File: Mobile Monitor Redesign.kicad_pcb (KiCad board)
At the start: 4 copper layers, 49 x 39.1 mm, 92 parts, among them J1 Conn_01x02_Pin, J2 Conn_01x08_Pin, J3 Conn_01x08_Pin, J4 USB_C_Receptacle_USB2.0_16P, J5 Conn_02x03_Odd_Even, J7 Conn_01x05_Pin, J8 Conn_01x06_Socket, Q1 2N7002, Q2 AO3401A, Q5 AO3401A, Q6 2N7002, U1 ATmega2560-16A, U10 BQ27441DRZR-G1A, U11 TPL5010, U2 DS3232M, U5 XL4005, U6 IP5306, U7 CH340C, U8 FP6298XR, U9 AMS1117-3.3, Y1 Crystal_GND23

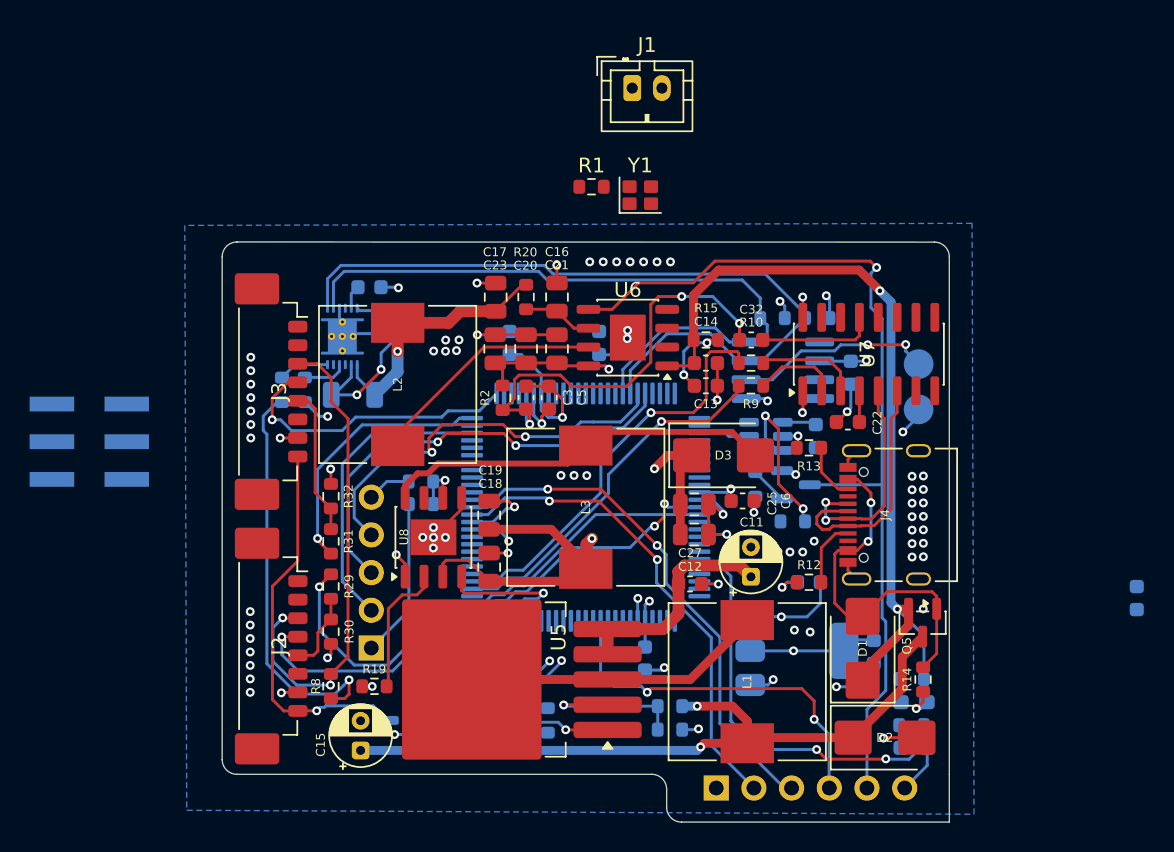
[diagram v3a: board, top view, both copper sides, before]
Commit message: cleaned up routes and added pads for SPI connections
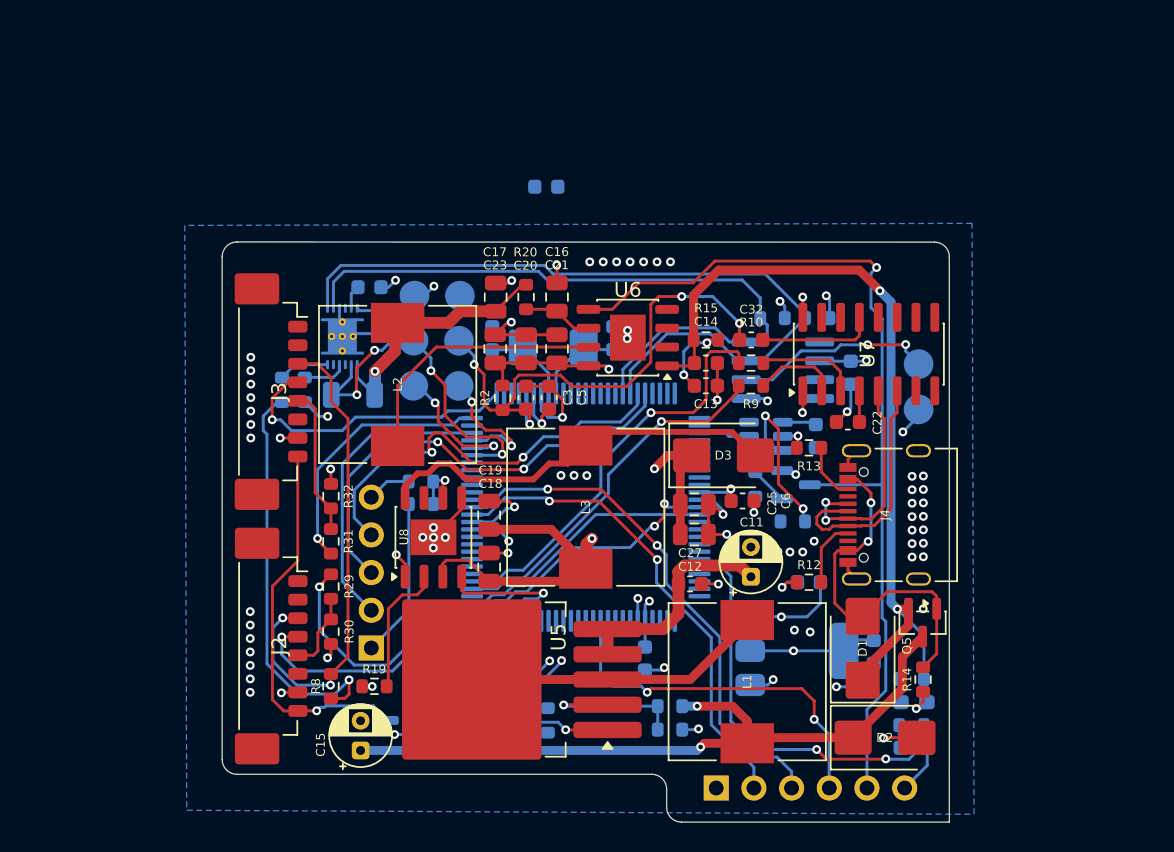
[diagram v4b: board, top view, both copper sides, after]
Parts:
- removed J1: Conn_01x02_Pin, Connector_JST:JST_PH_B2B-PH-K_1x02_P2.00mm_Vertical
- removed J5: Conn_02x03_Odd_Even, Connector_PinSocket_2.54mm:PinSocket_2x03_P2.54mm_Vertical_SMD
- removed R1: 1M, Resistor_SMD:R_0603_1608Metric
- removed Y1: Crystal_GND23, Crystal:Crystal_SMD_SeikoEpson_FA128-4Pin_2.0x1.6mm
- added 5V: TestPoint_Pad_D2.0mm, TestPoint:TestPoint_Pad_D2.0mm, B.Cu at (129.8, 84.8)
- added CLK: TestPoint_Pad_D2.0mm, TestPoint:TestPoint_Pad_D2.0mm, B.Cu at (129.8, 87.9)
- added GND: TestPoint_Pad_D2.0mm, TestPoint:TestPoint_Pad_D2.0mm, B.Cu at (132.9, 84.8)
- added MISO: TestPoint_Pad_D2.0mm, TestPoint:TestPoint_Pad_D2.0mm, B.Cu at (132.8, 90.9)
- added MOSI: TestPoint_Pad_D2.0mm, TestPoint:TestPoint_Pad_D2.0mm, B.Cu at (129.7, 90.9)
- added Y2: Crystal, Crystal:Crystal_SMD_Abracon_ABM3-2Pin_5.0x3.2mm, B.Cu at (139.2, 88.3)
- added rst: TestPoint_Pad_D2.0mm, TestPoint:TestPoint_Pad_D2.0mm, B.Cu at (132.8, 87.9)
- moved C30 48.5 mm to (138.7, 77.5), turned to 0 degrees
- moved C2 1.21 mm to (135.1, 87.7), turned to -90 degrees
- moved C1 1.00 mm to (143.2, 87.7), turned to 90 degrees
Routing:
- net SPI/CLK: track 0.00 -> 13.4 mm, vias 0 -> 2
- net SPI/MOSI: track 0.00 -> 9.25 mm, vias 0 -> 2
- net SPI/MISO: track 0.00 -> 9.19 mm, vias 0 -> 2
- net RESET: track 29.5 -> 35.9 mm, vias 3 -> 4
- net GND: track 107.3 -> 101.1 mm, vias 92 -> 87
- net Net-(U1-XTAL1): track 0.00 -> 6.03 mm
- net Net-(U1-XTAL2): track 0.00 -> 5.96 mm
- net /power/BATTERY_SEC: track 64.9 -> 67.0 mm
- net Net-(U6-SW): track 16.1 -> 18.0 mm
- net +5V: track 48.4 -> 50.0 mm, vias 12 -> 13
- net RXD1: track 27.3 -> 28.3 mm
- net Net-(D3-A): track 26.6 -> 27.5 mm
- net TXD1: track 30.6 -> 31.5 mm
- net TXD2: track 34.9 -> 35.6 mm

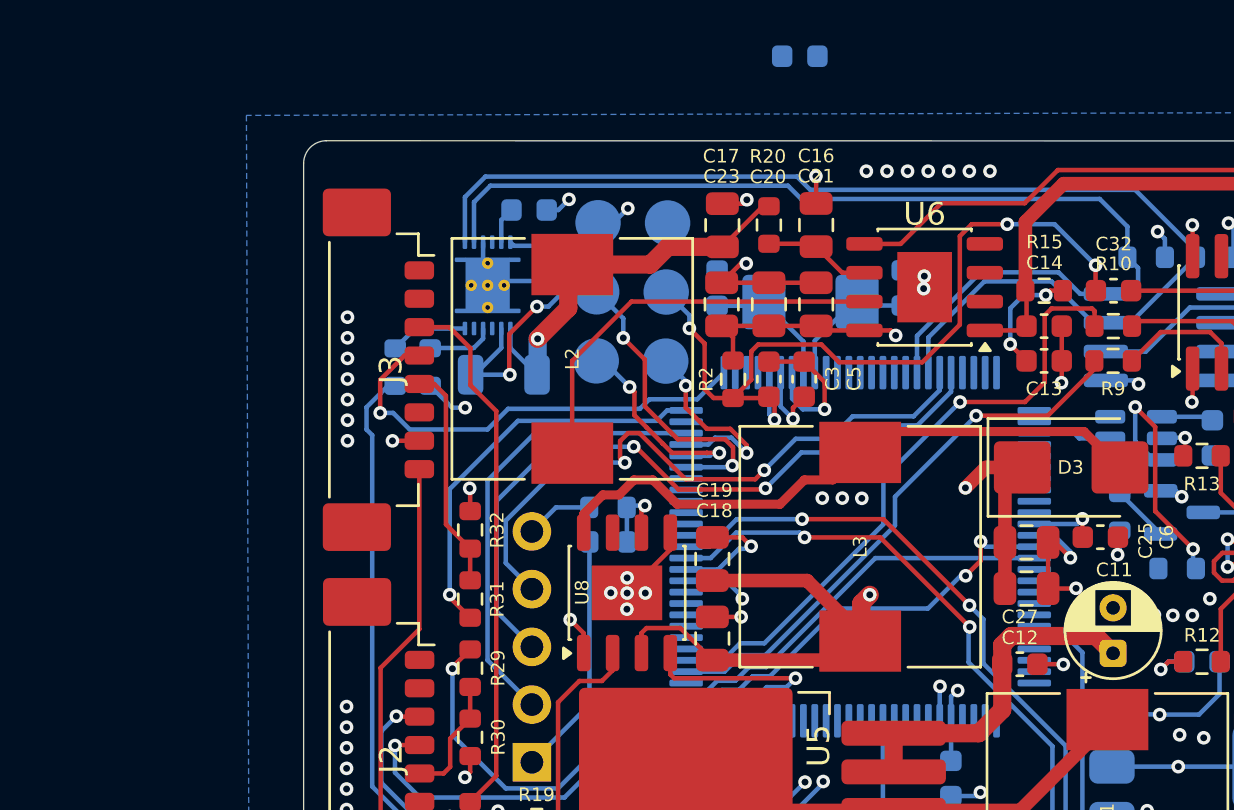
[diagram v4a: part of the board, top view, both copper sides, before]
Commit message: adjusted file locations of some 3d models so that the project is fully localized
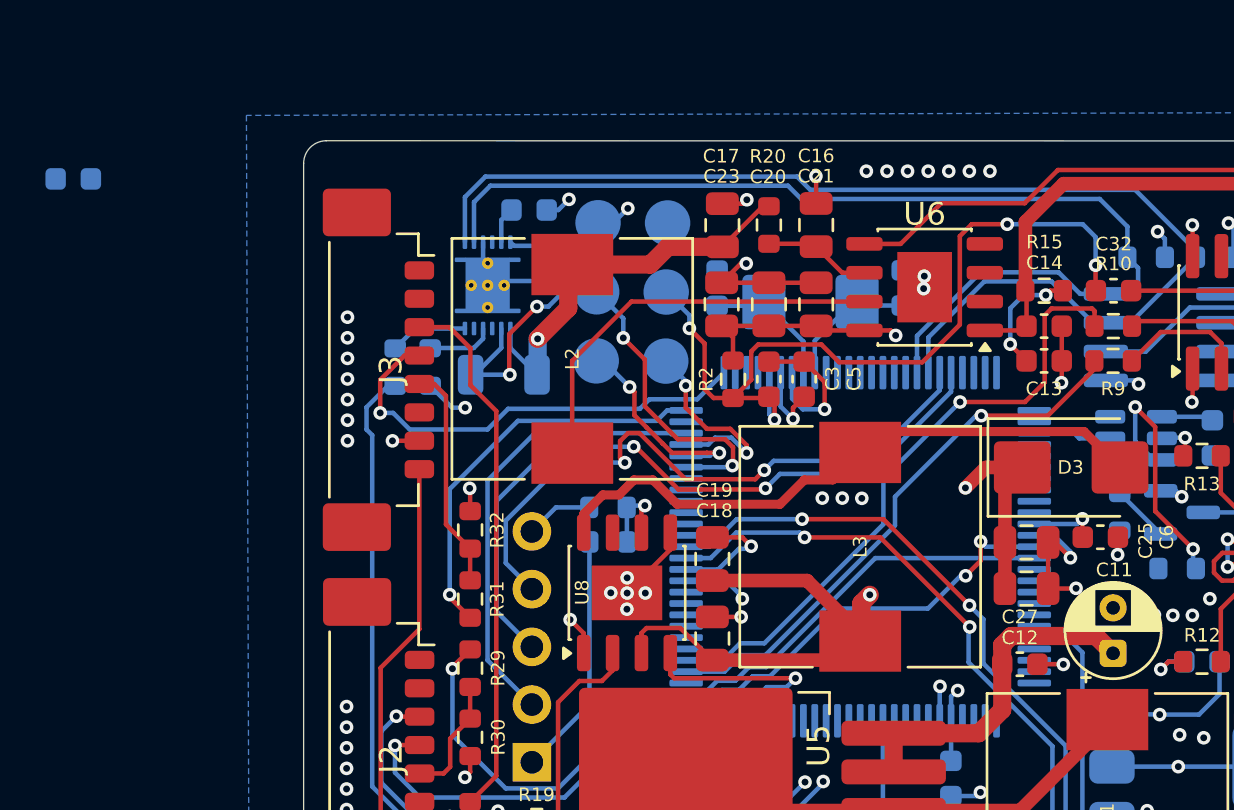
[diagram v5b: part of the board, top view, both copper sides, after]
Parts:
- vbat rtc: renamed from REF**
- moved C30 32.4 mm to (106.7, 82.9)
- renumbered REF** to gnd
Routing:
- net RESET: track 35.9 -> 36.6 mm

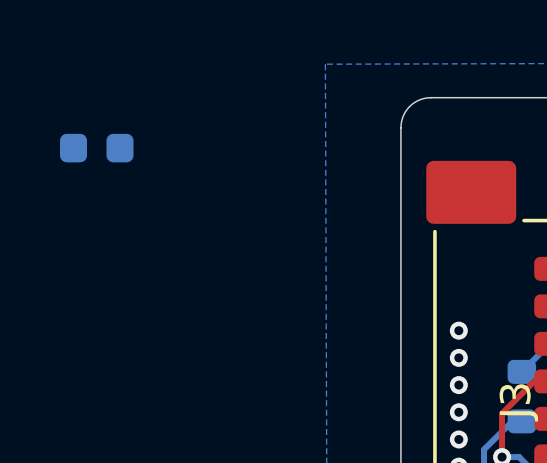
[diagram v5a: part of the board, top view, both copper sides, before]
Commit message: started on the enclosure designs
started on the enclosure designs
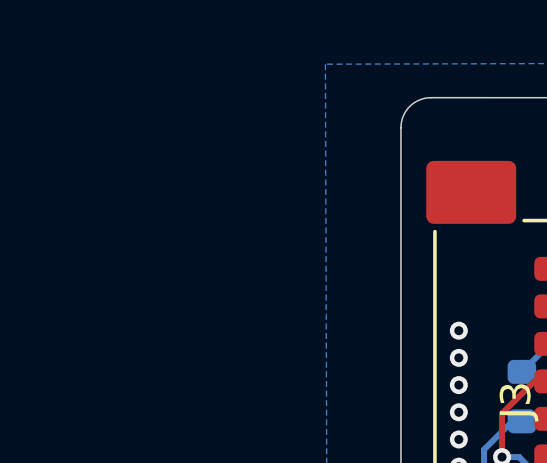
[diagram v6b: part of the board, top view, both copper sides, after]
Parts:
- removed C30: 100nF, Capacitor_SMD:C_0603_1608Metric
